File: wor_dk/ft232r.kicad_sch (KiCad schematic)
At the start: 9 parts, among them J501 USB_C_Receptacle_USB2.0_14P, U501 FT232RL

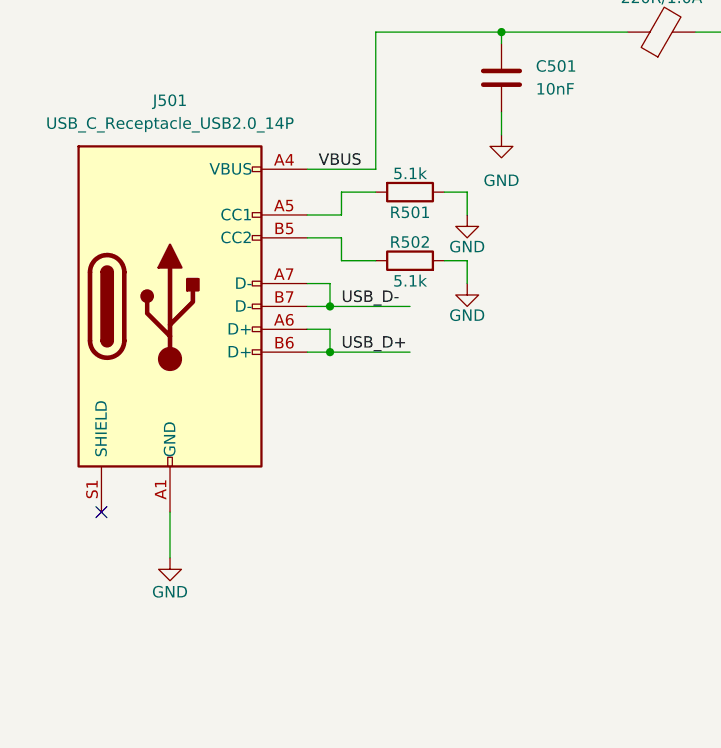
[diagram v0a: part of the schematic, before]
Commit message: wor_dk: add programmer
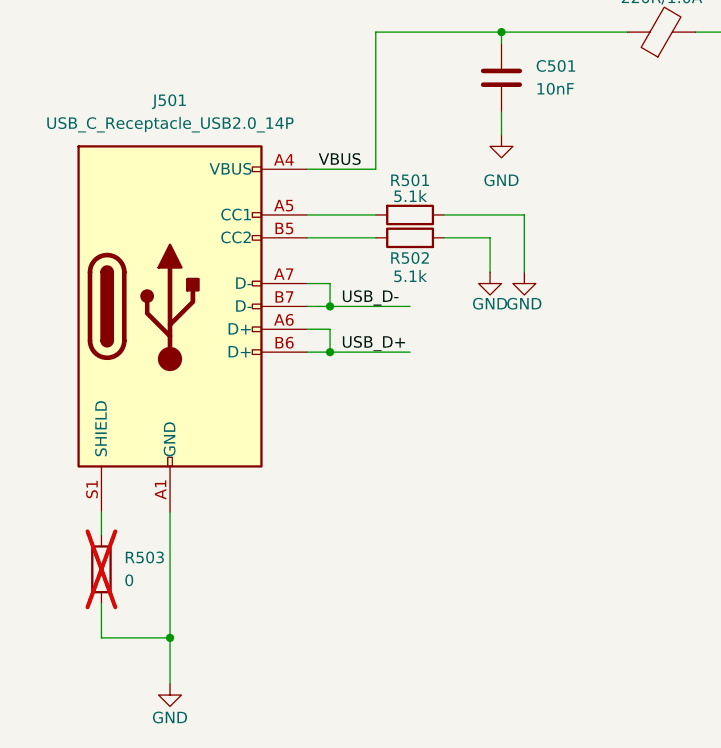
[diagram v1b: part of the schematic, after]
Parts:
- added R503: 0, symbol Device:R
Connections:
- net GND: now also R503.2
- net at J501.S1 (SHIELD): now also R503.1
- no-connect marks 15 -> 14
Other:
- title: (none) -> FT232 UART Interface
- moved on the sheet: R501, R502
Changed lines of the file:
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@@
 	(generator_version "8.0")
 	(paper "A4")
+	(title_block
+		(title "FT232 UART Interface")
+	)
 	(junction
 		(at 97.79 91.44)
@@
 	)
 	(junction
+		(at 80.01 128.27)
+		(diameter 0)
+		(color 0 0 0 0)
+	)
+	(junction
 		(at 194.31 60.96)
 		(diameter 0)
@@
 		(at 217.17 93.98)
 	)
-	(no_connect
-		(at 72.39 114.3)
-	)
 	(wire
 		(pts
@@
 	(wire
 		(pts
+			(xy 72.39 114.3) (xy 72.39 116.84)
+		)
+		(stroke
+			(width 0)
+			(type default)
+		)
+	)
+	(wire
+		(pts
 			(xy 199.39 60.96) (xy 199.39 73.66)
 		)
@@
 	(wire
 		(pts
-			(xy 99.06 86.36) (xy 102.87 86.36)
-		)
-		(stroke
-			(width 0)
-			(type default)
-		)
-	)
-	(wire
-		(pts
-			(xy 99.06 83.82) (xy 99.06 86.36)
+			(xy 72.39 128.27) (xy 80.01 128.27)
+		)
+		(stroke
+			(width 0)
+			(type default)
+		)
+	)
+	(wire
+		(pts
+			(xy 72.39 124.46) (xy 72.39 128.27)
 		)
 		(stroke
@@
 	(wire
 		(pts
-			(xy 99.06 81.28) (xy 95.25 81.28)
-		)
-		(stroke
-			(width 0)
-			(type default)
-		)
-	)
-	(wire
-		(pts
-			(xy 99.06 78.74) (xy 102.87 78.74)
+			(xy 95.25 81.28) (xy 102.87 81.28)
 		)
 		(stroke
@@
 	(wire
 		(pts
-			(xy 110.49 86.36) (xy 113.03 86.36)
+			(xy 110.49 83.82) (xy 115.57 83.82)
+		)
+		(stroke
+			(width 0)
+			(type default)
+		)
+	)
+	(wire
+		(pts
+			(xy 80.01 128.27) (xy 80.01 133.35)
 		)
 		(stroke
@@
 	(wire
 		(pts
-			(xy 110.49 78.74) (xy 113.03 78.74)
+			(xy 110.49 81.28) (xy 119.38 81.28)
 		)
 		(stroke
@@
 	(wire
 		(pts
-			(xy 99.06 78.74) (xy 99.06 81.28)
-		)
-		(stroke
-			(width 0)
-			(type default)
-		)
-	)
-	(wire
-		(pts
 			(xy 217.17 91.44) (xy 224.79 91.44)
 		)
@@
 	(wire
 		(pts
-			(xy 113.03 78.74) (xy 113.03 81.28)
+			(xy 119.38 81.28) (xy 119.38 87.63)
 		)
 		(stroke
@@
 	(wire
 		(pts
-			(xy 113.03 86.36) (xy 113.03 88.9)
+			(xy 115.57 83.82) (xy 115.57 87.63)
 		)
 		(stroke
@@
 	(wire
 		(pts
-			(xy 95.25 83.82) (xy 99.06 83.82)
-		)
-		(stroke
-			(width 0)
-			(type default)
-		)
-	)
-	(wire
-		(pts
-			(xy 80.01 114.3) (xy 80.01 119.38)
+			(xy 95.25 83.82) (xy 102.87 83.82)
+		)
+		(stroke
+			(width 0)
+			(type default)
+		)
+	)
+	(wire
+		(pts
+			(xy 80.01 114.3) (xy 80.01 128.27)
 		)
 		(stroke
@@
 	(symbol
 		(lib_id "power:GND")
-		(at 113.03 81.28 0)
+		(at 119.38 87.63 0)
 		(unit 1)
 		(exclude_from_sim no)
@@
 		(dnp no)
 		(property "Reference" "#PWR0501"
-			(at 113.03 87.63 0)
+			(at 119.38 93.98 0)
 			(effects
 				(font
@@
 		)
 		(property "Value" "GND"
-			(at 113.03 84.836 0)
+			(at 119.38 91.186 0)
 			(effects
 				(font
@@
 		)
 		(property "Footprint" ""
-			(at 113.03 81.28 0)
+			(at 119.38 87.63 0)
 			(effects
 				(font
@@
 		)
 		(property "Datasheet" ""
-			(at 113.03 81.28 0)
+			(at 119.38 87.63 0)
 			(effects
 				(font
@@
 		)
 		(property "Description" "Power symbol creates a global label with name \"GND\" , ground"
-			(at 113.03 81.28 0)
+			(at 119.38 87.63 0)
 			(effects
 				(font
@@
 	(symbol
 		(lib_id "power:GND")
-		(at 80.01 119.38 0)
+		(at 80.01 133.35 0)
 		(unit 1)
 		(exclude_from_sim no)
@@
 		(dnp no)
 		(property "Reference" "#PWR0503"
-			(at 80.01 125.73 0)
+			(at 80.01 139.7 0)
 			(effects
 				(font
@@
 		)
 		(property "Value" "GND"
-			(at 80.01 123.19 0)
+			(at 80.01 137.16 0)
 			(effects
 				(font
@@
 		)
 		(property "Footprint" ""
-			(at 80.01 119.38 0)
+			(at 80.01 133.35 0)
 			(effects
 				(font
@@
 		)
 		(property "Datasheet" ""
-			(at 80.01 119.38 0)
+			(at 80.01 133.35 0)
 			(effects
 				(font
@@
 		)
 		(property "Description" "Power symbol creates a global label with name \"GND\" , ground"
-			(at 80.01 119.38 0)
+			(at 80.01 133.35 0)
 			(effects
 				(font
@@
 	)
 	(symbol
+		(lib_id "Device:R")
+		(at 72.39 120.65 0)
+		(unit 1)
+		(exclude_from_sim no)
+		(in_bom yes)
+		(on_board yes)
+		(dnp yes)
+		(fields_autoplaced yes)
+		(property "Reference" "R503"
+			(at 74.93 119.3799 0)
+			(effects
+				(font
+					(size 1.27 1.27)
+				)
+				(justify left)
+			)
+		)
+		(property "Value" "0"
+			(at 74.93 121.9199 0)
+			(effects
+				(font
+					(size 1.27 1.27)
+				)
+				(justify left)
+			)
+		)
+		(property "Footprint" ""
+			(at 70.612 120.65 90)
+			(effects
+				(font
+					(size 1.27 1.27)
+				)
+				(hide yes)
+			)
+		)
+		(property "Datasheet" "~"
+			(at 72.39 120.65 0)
+			(effects
+				(font
+					(size 1.27 1.27)
+				)
+				(hide yes)
+			)
+		)
+		(property "Description" "Resistor"
+			(at 72.39 120.65 0)
+			(effects
+				(font
+					(size 1.27 1.27)
+				)
+				(hide yes)
+			)
+		)
+		(pin "1"
+		)
+		(pin "2"
+		)
+		(instances
+			(project ""
+				(path "/8d3147eb-060b-4f65-bf42-ed06a58b21ba/711499aa-b4ff-4669-a7c0-a5db1aab8120"
+					(reference "R503")
+					(unit 1)
+				)
+			)
+		)
+	)
+	(symbol
 		(lib_id "Device:C")
 		(at 153.67 66.04 0)
@@
 	(symbol
 		(lib_id "Device:R")
-		(at 106.68 86.36 90)
+		(at 106.68 83.82 90)
 		(unit 1)
 		(exclude_from_sim no)
@@
 		(dnp no)
 		(property "Reference" "R502"
-			(at 106.68 84.328 90)
+			(at 106.68 86.106 90)
 			(effects
 				(font
@@
 		)
 		(property "Value" "5.1k"
-			(at 106.68 88.646 90)
+			(at 106.68 88.138 90)
 			(effects
 				(font
@@
 		)
 		(property "Footprint" ""
-			(at 106.68 88.138 90)
+			(at 106.68 85.598 90)
 			(effects
 				(font
@@
 		)
 		(property "Datasheet" "~"
-			(at 106.68 86.36 0)
+			(at 106.68 83.82 0)
 			(effects
 				(font
@@
 		)
 		(property "Description" "Resistor"
-			(at 106.68 86.36 0)
+			(at 106.68 83.82 0)
 			(effects
 				(font
@@
 	(symbol
 		(lib_id "Device:R")
-		(at 106.68 78.74 270)
+		(at 106.68 81.28 270)
 		(unit 1)
 		(exclude_from_sim no)
@@
 		(dnp no)
 		(property "Reference" "R501"
-			(at 106.68 81.026 90)
+			(at 106.68 77.47 90)
 			(effects
 				(font
@@
 		)
 		(property "Value" "5.1k"
-			(at 106.68 76.708 90)
+			(at 106.68 79.248 90)
 			(effects
 				(font
@@
 		)
 		(property "Footprint" ""
-			(at 106.68 76.962 90)
+			(at 106.68 79.502 90)
 			(effects
 				(font
@@
 		)
 		(property "Datasheet" "~"
-			(at 106.68 78.74 0)
+			(at 106.68 81.28 0)
 			(effects
 				(font
@@
 		)
 		(property "Description" "Resistor"
-			(at 106.68 78.74 0)
+			(at 106.68 81.28 0)
 			(effects
 				(font
@@
 	(symbol
 		(lib_id "power:GND")
-		(at 113.03 88.9 0)
+		(at 115.57 87.63 0)
 		(unit 1)
 		(exclude_from_sim no)
@@
 		(dnp no)
 		(property "Reference" "#PWR0502"
-			(at 113.03 95.25 0)
+			(at 115.57 93.98 0)
 			(effects
 				(font
@@
 		)
 		(property "Value" "GND"
-			(at 113.03 92.456 0)
+			(at 115.57 91.186 0)
 			(effects
 				(font
@@
 		)
 		(property "Footprint" ""
-			(at 113.03 88.9 0)
+			(at 115.57 87.63 0)
 			(effects
 				(font
@@
 		)
 		(property "Datasheet" ""
-			(at 113.03 88.9 0)
+			(at 115.57 87.63 0)
 			(effects
 				(font
@@
 		)
 		(property "Description" "Power symbol creates a global label with name \"GND\" , ground"
-			(at 113.03 88.9 0)
-			(effects
-				(font
+			(at 115.57 87.63 0)
+			(effects
+				(font

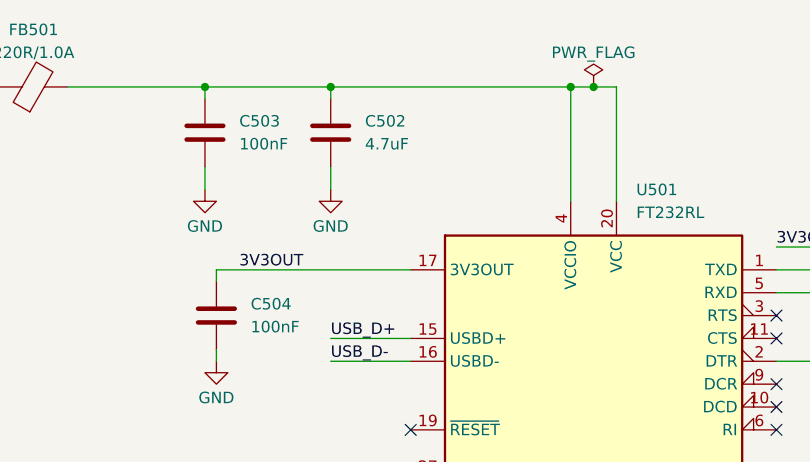
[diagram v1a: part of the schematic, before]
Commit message: wor_dk: FT232: connect VCCIO to 3V3OUT for 3V3 GPIO drive
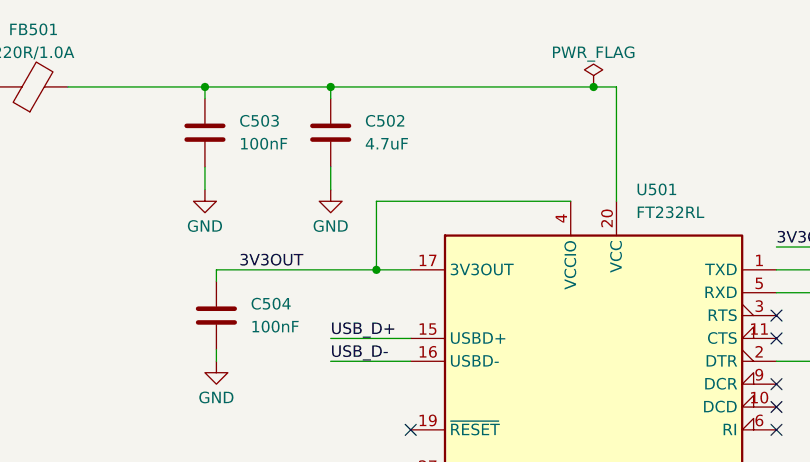
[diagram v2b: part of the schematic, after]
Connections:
- net 3V3OUT: now also U501.4 (VCCIO)
- net at C502.1, C503.1, FB501.2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: no longer U501.4 (VCCIO)
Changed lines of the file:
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@@
+	)
+	(junction
+		(at 172.72 81.28)
+		(diameter 0)
+		(color 0 0 0 0)
 	)
 	(junction
@@
 	)
 	(junction
-		(at 194.31 60.96)
-		(diameter 0)
-		(color 0 0 0 0)
-	)
-	(junction
 		(at 198.12 127)
 		(diameter 0)
@@
 	(wire
 		(pts
+			(xy 172.72 81.28) (xy 176.53 81.28)
+		)
+		(stroke
+			(width 0)
+			(type default)
+		)
+	)
+	(wire
+		(pts
 			(xy 95.25 81.28) (xy 102.87 81.28)
 		)
@@
 	(wire
 		(pts
+			(xy 172.72 73.66) (xy 172.72 81.28)
+		)
+		(stroke
+			(width 0)
+			(type default)
+		)
+	)
+	(wire
+		(pts
 			(xy 80.01 128.27) (xy 80.01 133.35)
 		)
@@
 	(wire
 		(pts
-			(xy 167.64 60.96) (xy 194.31 60.96)
+			(xy 167.64 60.96) (xy 196.85 60.96)
 		)
 		(stroke
@@
 	(wire
 		(pts
-			(xy 194.31 60.96) (xy 196.85 60.96)
-		)
-		(stroke
-			(width 0)
-			(type default)
-		)
-	)
-	(wire
-		(pts
 			(xy 196.85 127) (xy 198.12 127)
 		)
@@
 	(wire
 		(pts
-			(xy 154.94 81.28) (xy 176.53 81.28)
+			(xy 154.94 81.28) (xy 172.72 81.28)
 		)
 		(stroke
@@
 	(wire
 		(pts
-			(xy 194.31 60.96) (xy 194.31 73.66)
-		)
-		(stroke
+			(xy 194.31 73.66) (xy 172.72 73.66)
+		)
+		(stroke

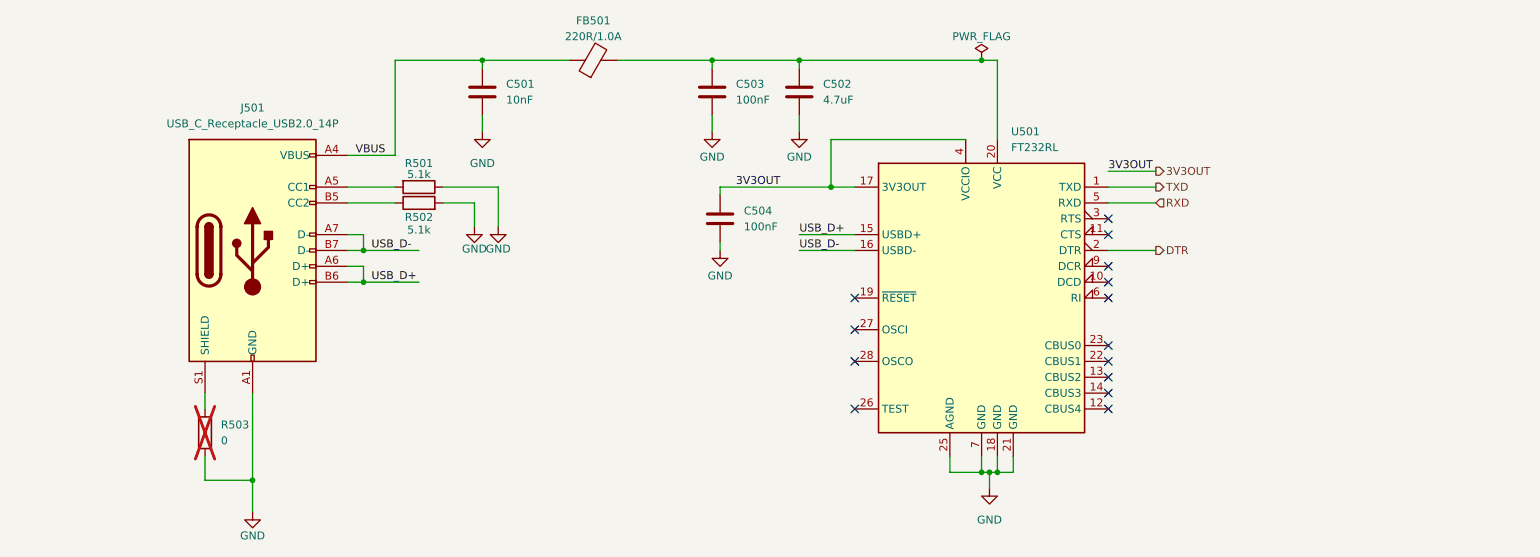
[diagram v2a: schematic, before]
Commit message: wor_dk: FT232: add LEDs for UART TX/RX and PWREN
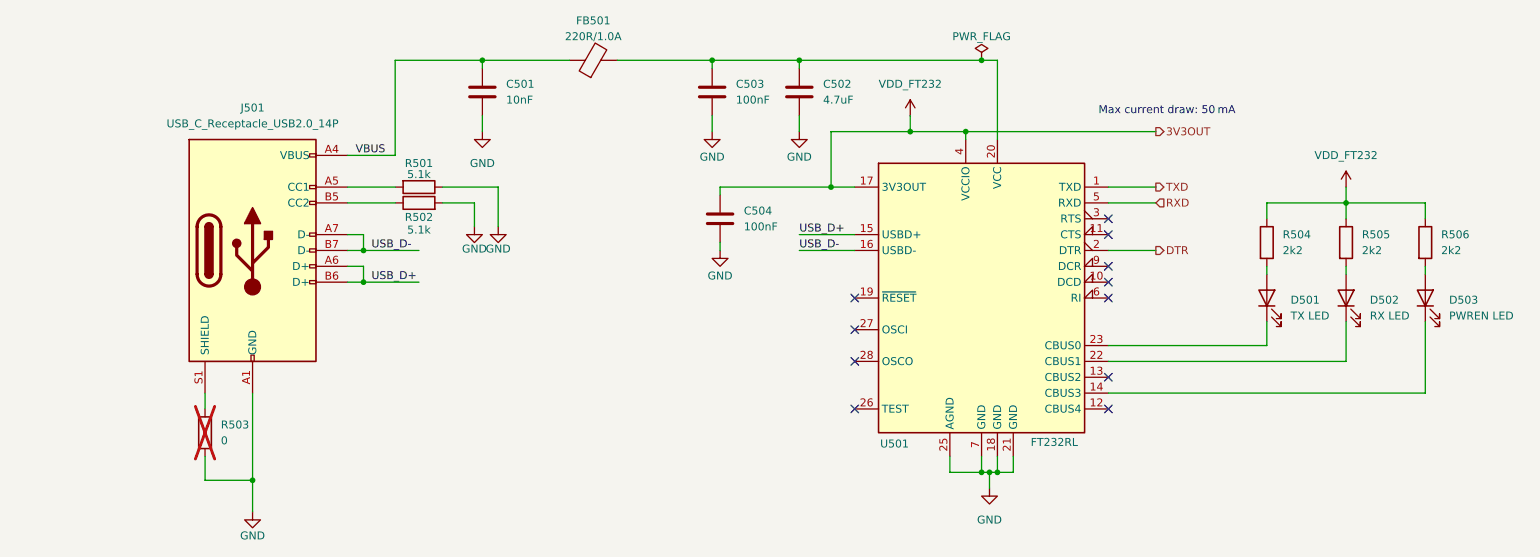
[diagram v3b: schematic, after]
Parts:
- added D501: TX LED, LED_SMD:LED_0805_2012Metric, symbol Device:LED
- added D502: RX LED, LED_SMD:LED_0805_2012Metric, symbol Device:LED
- added D503: PWREN LED, LED_SMD:LED_0805_2012Metric, symbol Device:LED
- added R504, R505, R506: 2k2, Resistor_SMD:R_0402_1005Metric, symbol Device:R
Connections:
- net at U501.14 (CBUS3): now also D503.1 (K)
- net at U501.22 (CBUS1): now also D502.1 (K)
- net at U501.23 (CBUS0): now also D501.1 (K)
- net 3V3OUT renamed VDD_FT232
- net VDD_FT232: now also R504.1, R505.1, R506.1
- new net: D501.2 (A), R504.2
- new net: D502.2 (A), R505.2
- new net: D503.2 (A), R506.2
- no-connect marks 14 -> 11
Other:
- note added: "Max current draw: 50 mA"
